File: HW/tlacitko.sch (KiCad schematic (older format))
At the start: 2 parts, among them SW2 button

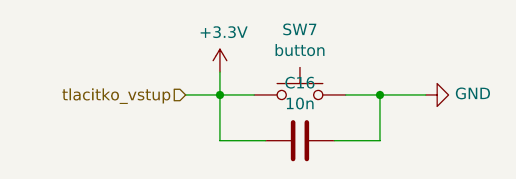
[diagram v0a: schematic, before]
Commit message: repair package of TP4056
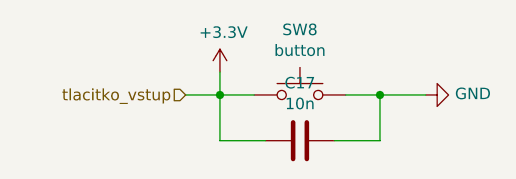
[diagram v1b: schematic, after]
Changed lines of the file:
@@
 $Descr A4 11693 8268
 encoding utf-8
-Sheet 9 44
+Sheet 10 44
 Title ""
 Date ""
@@
 AR Path="/5FB92F8B/5F76F2AA/5F76AB3F" Ref="SW7"  Part="1"
 AR Path="/5FB92F8B/5F76F385/5F76AB3F" Ref="SW8"  Part="1"
-F 0 "SW7" H 3750 3085 50  0000 C CNN
+F 0 "SW8" H 3750 3085 50  0000 C CNN
 F 1 "button" H 3750 2994 50  0000 C CNN
 F 2 "Button_Switch_THT:SW_Tactile_Straight_KSL0Axx1LFTR" H 3750 3000 50  0001 C CNN
@@
 AR Path="/5FB92F8B/5F76F2AA/5F76AB45" Ref="C16"  Part="1"
 AR Path="/5FB92F8B/5F76F385/5F76AB45" Ref="C17"  Part="1"
-F 0 "C16" V 3498 3000 50  0000 C CNN
+F 0 "C17" V 3498 3000 50  0000 C CNN
 F 1 "10n" V 3589 3000 50  0000 C CNN
 F 2 "Capacitor_SMD:C_0402_1005Metric" H 3788 2850 50  0001 C CNN
@@
 AR Path="/5FB92F8B/5F76F2AA/5F76AB53" Ref="#PWR0125"  Part="1"
 AR Path="/5FB92F8B/5F76F385/5F76AB53" Ref="#PWR0127"  Part="1"
-F 0 "#PWR0125" H 4300 2550 50  0001 C CNN
+F 0 "#PWR0127" H 4300 2550 50  0001 C CNN
 F 1 "GND" V 4305 2672 50  0000 R CNN
 F 2 "" H 4300 2800 50  0001 C CNN
@@
 AR Path="/5FB92F8B/5F76F2AA/5F76AB5B" Ref="#PWR0126"  Part="1"
 AR Path="/5FB92F8B/5F76F385/5F76AB5B" Ref="#PWR0128"  Part="1"
-F 0 "#PWR0126" H 3400 2550 50  0001 C CNN
+F 0 "#PWR0128" H 3400 2550 50  0001 C CNN
 F 1 "+3.3V" H 3415 2873 50  0000 C CNN
 F 2 "" H 3400 2700 50  0001 C CNN

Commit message: repair mistake with buttons
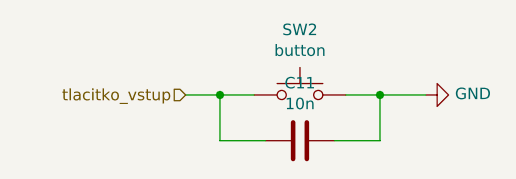
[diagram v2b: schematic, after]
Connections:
- net +3V3 renamed tlacitko_vstup
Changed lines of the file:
@@
 $Descr A4 11693 8268
 encoding utf-8
-Sheet 10 44
+Sheet 4 44
 Title ""
 Date ""
@@
 AR Path="/5FB92F8B/5F76F2AA/5F76AB3F" Ref="SW7"  Part="1"
 AR Path="/5FB92F8B/5F76F385/5F76AB3F" Ref="SW8"  Part="1"
-F 0 "SW8" H 3750 3085 50  0000 C CNN
+F 0 "SW2" H 3750 3085 50  0000 C CNN
 F 1 "button" H 3750 2994 50  0000 C CNN
 F 2 "Button_Switch_THT:SW_Tactile_Straight_KSL0Axx1LFTR" H 3750 3000 50  0001 C CNN
@@
 AR Path="/5FB92F8B/5F76F2AA/5F76AB45" Ref="C16"  Part="1"
 AR Path="/5FB92F8B/5F76F385/5F76AB45" Ref="C17"  Part="1"
-F 0 "C17" V 3498 3000 50  0000 C CNN
+F 0 "C11" V 3498 3000 50  0000 C CNN
 F 1 "10n" V 3589 3000 50  0000 C CNN
 F 2 "Capacitor_SMD:C_0402_1005Metric" H 3788 2850 50  0001 C CNN
@@
 AR Path="/5FB92F8B/5F76F2AA/5F76AB53" Ref="#PWR0125"  Part="1"
 AR Path="/5FB92F8B/5F76F385/5F76AB53" Ref="#PWR0127"  Part="1"
-F 0 "#PWR0127" H 4300 2550 50  0001 C CNN
+F 0 "#PWR0115" H 4300 2550 50  0001 C CNN
 F 1 "GND" V 4305 2672 50  0000 R CNN
 F 2 "" H 4300 2800 50  0001 C CNN
@@
 	4300 2800 4100 2800
 Connection ~ 4100 2800
-$Comp
-L power:+3.3V #PWR?
-U 1 1 5F76AB5B
-P 3400 2700
-AR Path="/5F76AB5B" Ref="#PWR?"  Part="1"
-AR Path="/5FB92F8B/5F76AB5B" Ref="#PWR?"  Part="1"
-AR Path="/5FB92F8B/5F768D65/5F76AB5B" Ref="#PWR0116"  Part="1"
-AR Path="/5FB92F8B/5F76BB44/5F76AB5B" Ref="#PWR0118"  Part="1"
-AR Path="/5FB92F8B/5F76DF12/5F76AB5B" Ref="#PWR0120"  Part="1"
-AR Path="/5FB92F8B/5F76E918/5F76AB5B" Ref="#PWR0122"  Part="1"
-AR Path="/5FB92F8B/5F76EE0D/5F76AB5B" Ref="#PWR0124"  Part="1"
-AR Path="/5FB92F8B/5F76F2AA/5F76AB5B" Ref="#PWR0126"  Part="1"
-AR Path="/5FB92F8B/5F76F385/5F76AB5B" Ref="#PWR0128"  Part="1"
-F 0 "#PWR0128" H 3400 2550 50  0001 C CNN
-F 1 "+3.3V" H 3415 2873 50  0000 C CNN
-F 2 "" H 3400 2700 50  0001 C CNN
-F 3 "" H 3400 2700 50  0001 C CNN
-	1    3400 2700
-	1    0    0    -1
-$EndComp
-Wire Wire Line
-	3400 2700 3400 2800
 Text HLabel 3250 2800 0    50   Input ~ 0
 tlacitko_vstup

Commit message: make smaller test version, start routing
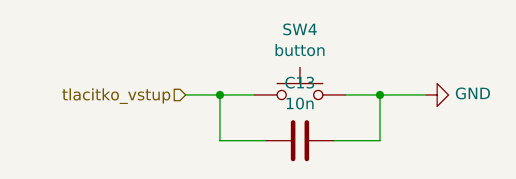
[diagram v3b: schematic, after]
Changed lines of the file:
@@
 $Descr A4 11693 8268
 encoding utf-8
-Sheet 4 44
+Sheet 6 34
 Title ""
 Date ""
@@
 AR Path="/5FB92F8B/5F76F2AA/5F76AB3F" Ref="SW7"  Part="1"
 AR Path="/5FB92F8B/5F76F385/5F76AB3F" Ref="SW8"  Part="1"
-F 0 "SW2" H 3750 3085 50  0000 C CNN
+AR Path="/5FB92F8B/5F896DB4/5F76AB3F" Ref="SW9"  Part="1"
+AR Path="/5FB92F8B/5F896DD0/5F76AB3F" Ref="SW10"  Part="1"
+AR Path="/5FB92F8B/5F896DFE/5F76AB3F" Ref="SW11"  Part="1"
+AR Path="/5FB92F8B/5F896E12/5F76AB3F" Ref="SW12"  Part="1"
+F 0 "SW4" H 3750 3085 50  0000 C CNN
 F 1 "button" H 3750 2994 50  0000 C CNN
 F 2 "Button_Switch_THT:SW_Tactile_Straight_KSL0Axx1LFTR" H 3750 3000 50  0001 C CNN
@@
 AR Path="/5FB92F8B/5F76F2AA/5F76AB45" Ref="C16"  Part="1"
 AR Path="/5FB92F8B/5F76F385/5F76AB45" Ref="C17"  Part="1"
-F 0 "C11" V 3498 3000 50  0000 C CNN
+AR Path="/5FB92F8B/5F896DB4/5F76AB45" Ref="C30"  Part="1"
+AR Path="/5FB92F8B/5F896DD0/5F76AB45" Ref="C32"  Part="1"
+AR Path="/5FB92F8B/5F896DFE/5F76AB45" Ref="C34"  Part="1"
+AR Path="/5FB92F8B/5F896E12/5F76AB45" Ref="C36"  Part="1"
+F 0 "C13" V 3498 3000 50  0000 C CNN
 F 1 "10n" V 3589 3000 50  0000 C CNN
 F 2 "Capacitor_SMD:C_0402_1005Metric" H 3788 2850 50  0001 C CNN
@@
 AR Path="/5FB92F8B/5F76F2AA/5F76AB53" Ref="#PWR0125"  Part="1"
 AR Path="/5FB92F8B/5F76F385/5F76AB53" Ref="#PWR0127"  Part="1"
-F 0 "#PWR0115" H 4300 2550 50  0001 C CNN
+AR Path="/5FB92F8B/5F896DB4/5F76AB53" Ref="#PWR0116"  Part="1"
+AR Path="/5FB92F8B/5F896DD0/5F76AB53" Ref="#PWR0118"  Part="1"
+AR Path="/5FB92F8B/5F896DFE/5F76AB53" Ref="#PWR0120"  Part="1"
+AR Path="/5FB92F8B/5F896E12/5F76AB53" Ref="#PWR0122"  Part="1"
+F 0 "#PWR0119" H 4300 2550 50  0001 C CNN
 F 1 "GND" V 4305 2672 50  0000 R CNN
 F 2 "" H 4300 2800 50  0001 C CNN

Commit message: continuation routing
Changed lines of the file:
@@
 $Descr A4 11693 8268
 encoding utf-8
-Sheet 6 34
+Sheet 8 34
 Title ""
 Date ""
@@
 AR Path="/5FB92F8B/5F896DFE/5F76AB3F" Ref="SW11"  Part="1"
 AR Path="/5FB92F8B/5F896E12/5F76AB3F" Ref="SW12"  Part="1"
-F 0 "SW4" H 3750 3085 50  0000 C CNN
+F 0 "SW6" H 3750 3085 50  0000 C CNN
 F 1 "button" H 3750 2994 50  0000 C CNN
 F 2 "Button_Switch_THT:SW_Tactile_Straight_KSL0Axx1LFTR" H 3750 3000 50  0001 C CNN
@@
 AR Path="/5FB92F8B/5F896DFE/5F76AB45" Ref="C34"  Part="1"
 AR Path="/5FB92F8B/5F896E12/5F76AB45" Ref="C36"  Part="1"
-F 0 "C13" V 3498 3000 50  0000 C CNN
+F 0 "C15" V 3498 3000 50  0000 C CNN
 F 1 "10n" V 3589 3000 50  0000 C CNN
 F 2 "Capacitor_SMD:C_0402_1005Metric" H 3788 2850 50  0001 C CNN
@@
 AR Path="/5FB92F8B/5F896DFE/5F76AB53" Ref="#PWR0120"  Part="1"
 AR Path="/5FB92F8B/5F896E12/5F76AB53" Ref="#PWR0122"  Part="1"
-F 0 "#PWR0119" H 4300 2550 50  0001 C CNN
+F 0 "#PWR0122" H 4300 2550 50  0001 C CNN
 F 1 "GND" V 4305 2672 50  0000 R CNN
 F 2 "" H 4300 2800 50  0001 C CNN

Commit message: change structure of buttons, switching power
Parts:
- removed C11: 10n, Capacitor_SMD:C_0402_1005Metric, symbol Device:C
- removed SW2: button, Button_Switch_THT:SW_Tactile_Straight_KSL0Axx1LFTR, symbol Switch:SW_Push
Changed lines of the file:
@@
 $Descr A4 11693 8268
 encoding utf-8
-Sheet 8 34
+Sheet 4 29
 Title ""
 Date ""
@@
 Comment4 ""
 $EndDescr
-$Comp
-L Switch:SW_Push SW?
-U 1 1 5F76AB3F
-P 3750 2800
-AR Path="/5F76AB3F" Ref="SW?"  Part="1"
-AR Path="/5FB92F8B/5F76AB3F" Ref="SW?"  Part="1"
-AR Path="/5FB92F8B/5F768D65/5F76AB3F" Ref="SW2"  Part="1"
-AR Path="/5FB92F8B/5F76BB44/5F76AB3F" Ref="SW3"  Part="1"
-AR Path="/5FB92F8B/5F76DF12/5F76AB3F" Ref="SW4"  Part="1"
-AR Path="/5FB92F8B/5F76E918/5F76AB3F" Ref="SW5"  Part="1"
-AR Path="/5FB92F8B/5F76EE0D/5F76AB3F" Ref="SW6"  Part="1"
-AR Path="/5FB92F8B/5F76F2AA/5F76AB3F" Ref="SW7"  Part="1"
-AR Path="/5FB92F8B/5F76F385/5F76AB3F" Ref="SW8"  Part="1"
-AR Path="/5FB92F8B/5F896DB4/5F76AB3F" Ref="SW9"  Part="1"
-AR Path="/5FB92F8B/5F896DD0/5F76AB3F" Ref="SW10"  Part="1"
-AR Path="/5FB92F8B/5F896DFE/5F76AB3F" Ref="SW11"  Part="1"
-AR Path="/5FB92F8B/5F896E12/5F76AB3F" Ref="SW12"  Part="1"
-F 0 "SW6" H 3750 3085 50  0000 C CNN
-F 1 "button" H 3750 2994 50  0000 C CNN
-F 2 "Button_Switch_THT:SW_Tactile_Straight_KSL0Axx1LFTR" H 3750 3000 50  0001 C CNN
-F 3 "~" H 3750 3000 50  0001 C CNN
-F 4 "ručně" H 3750 2800 50  0001 C CNN "LCSC"
-	1    3750 2800
-	1    0    0    -1
-$EndComp
-$Comp
-L Device:C C?
-U 1 1 5F76AB45
-P 3750 3000
-AR Path="/5F76AB45" Ref="C?"  Part="1"
-AR Path="/5FB92F8B/5F76AB45" Ref="C?"  Part="1"
-AR Path="/5FB92F8B/5F768D65/5F76AB45" Ref="C11"  Part="1"
-AR Path="/5FB92F8B/5F76BB44/5F76AB45" Ref="C12"  Part="1"
-AR Path="/5FB92F8B/5F76DF12/5F76AB45" Ref="C13"  Part="1"
-AR Path="/5FB92F8B/5F76E918/5F76AB45" Ref="C14"  Part="1"
-AR Path="/5FB92F8B/5F76EE0D/5F76AB45" Ref="C15"  Part="1"
-AR Path="/5FB92F8B/5F76F2AA/5F76AB45" Ref="C16"  Part="1"
-AR Path="/5FB92F8B/5F76F385/5F76AB45" Ref="C17"  Part="1"
-AR Path="/5FB92F8B/5F896DB4/5F76AB45" Ref="C30"  Part="1"
-AR Path="/5FB92F8B/5F896DD0/5F76AB45" Ref="C32"  Part="1"
-AR Path="/5FB92F8B/5F896DFE/5F76AB45" Ref="C34"  Part="1"
-AR Path="/5FB92F8B/5F896E12/5F76AB45" Ref="C36"  Part="1"
-F 0 "C15" V 3498 3000 50  0000 C CNN
-F 1 "10n" V 3589 3000 50  0000 C CNN
-F 2 "Capacitor_SMD:C_0402_1005Metric" H 3788 2850 50  0001 C CNN
-F 3 "~" H 3750 3000 50  0001 C CNN
-F 4 "C15195" H 3750 3000 50  0001 C CNN "LCSC"
-	1    3750 3000
-	0    1    1    0
-$EndComp
-Wire Wire Line
-	3550 2800 3400 2800
-Wire Wire Line
-	3400 2800 3400 3000
-Wire Wire Line
-	3400 3000 3600 3000
-Wire Wire Line
-	3250 2800 3400 2800
-Connection ~ 3400 2800
-Wire Wire Line
-	3950 2800 4100 2800
-Wire Wire Line
-	4100 2800 4100 3000
-Wire Wire Line
-	4100 3000 3900 3000
-$Comp
-L power:GND #PWR?
-U 1 1 5F76AB53
-P 4300 2800
-AR Path="/5F76AB53" Ref="#PWR?"  Part="1"
-AR Path="/5FB92F8B/5F76AB53" Ref="#PWR?"  Part="1"
-AR Path="/5FB92F8B/5F768D65/5F76AB53" Ref="#PWR0115"  Part="1"
-AR Path="/5FB92F8B/5F76BB44/5F76AB53" Ref="#PWR0117"  Part="1"
-AR Path="/5FB92F8B/5F76DF12/5F76AB53" Ref="#PWR0119"  Part="1"
-AR Path="/5FB92F8B/5F76E918/5F76AB53" Ref="#PWR0121"  Part="1"
-AR Path="/5FB92F8B/5F76EE0D/5F76AB53" Ref="#PWR0123"  Part="1"
-AR Path="/5FB92F8B/5F76F2AA/5F76AB53" Ref="#PWR0125"  Part="1"
-AR Path="/5FB92F8B/5F76F385/5F76AB53" Ref="#PWR0127"  Part="1"
-AR Path="/5FB92F8B/5F896DB4/5F76AB53" Ref="#PWR0116"  Part="1"
-AR Path="/5FB92F8B/5F896DD0/5F76AB53" Ref="#PWR0118"  Part="1"
-AR Path="/5FB92F8B/5F896DFE/5F76AB53" Ref="#PWR0120"  Part="1"
-AR Path="/5FB92F8B/5F896E12/5F76AB53" Ref="#PWR0122"  Part="1"
-F 0 "#PWR0122" H 4300 2550 50  0001 C CNN
-F 1 "GND" V 4305 2672 50  0000 R CNN
-F 2 "" H 4300 2800 50  0001 C CNN
-F 3 "" H 4300 2800 50  0001 C CNN
-	1    4300 2800
-	0    -1   -1   0
-$EndComp
-Wire Wire Line
-	4300 2800 4100 2800
-Connection ~ 4100 2800
-Text HLabel 3250 2800 0    50   Input ~ 0
-tlacitko_vstup
 $EndSCHEMATC
